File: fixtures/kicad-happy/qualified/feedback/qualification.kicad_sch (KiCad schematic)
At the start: 9 parts, among them J1 USB_B, J2 Power, U1 LM317, U2 Load

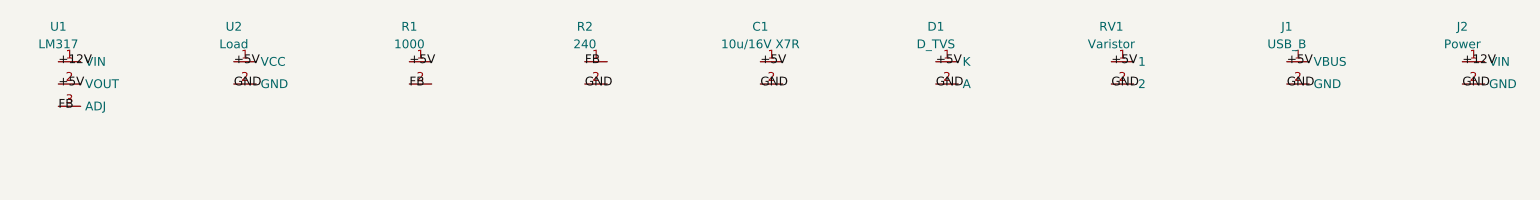
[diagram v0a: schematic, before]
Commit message: Qualify derating, thermal and EMC adapters with source-backed boundary evidence
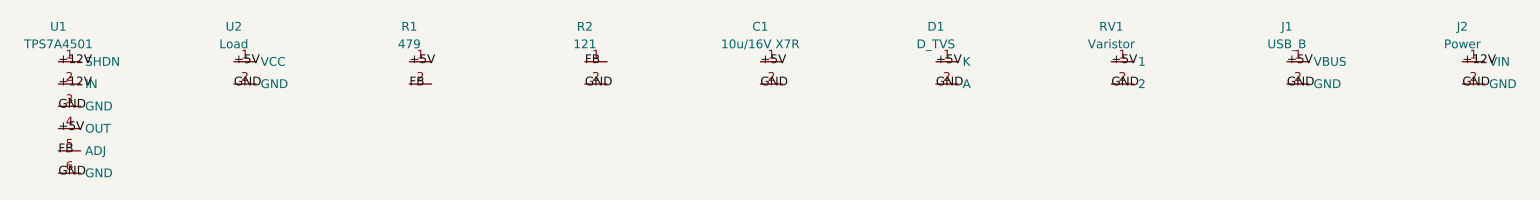
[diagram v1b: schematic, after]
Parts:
- R1: value 1000 -> 479
- R2: value 240 -> 121
- U1: value LM317 -> TPS7A4501; symbol Regulator_Linear:LM317 -> Regulator_Linear:TPS7A4501
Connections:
- net +12V: now also U1.2 (IN)
- net +5V: now also U1.4 (OUT); no longer U1.2 (VOUT)
- net FB: now also U1.5 (ADJ); no longer U1.3 (ADJ)
- net GND: now also U1.3 (GND), U1.6 (GND)
